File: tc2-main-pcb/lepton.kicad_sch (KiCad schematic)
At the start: 34 parts, among them U110 TD6810, U111 TD6810, U112 ME6216A28XG, U113 3N25000G33YC, U114 Flir_LEPTON

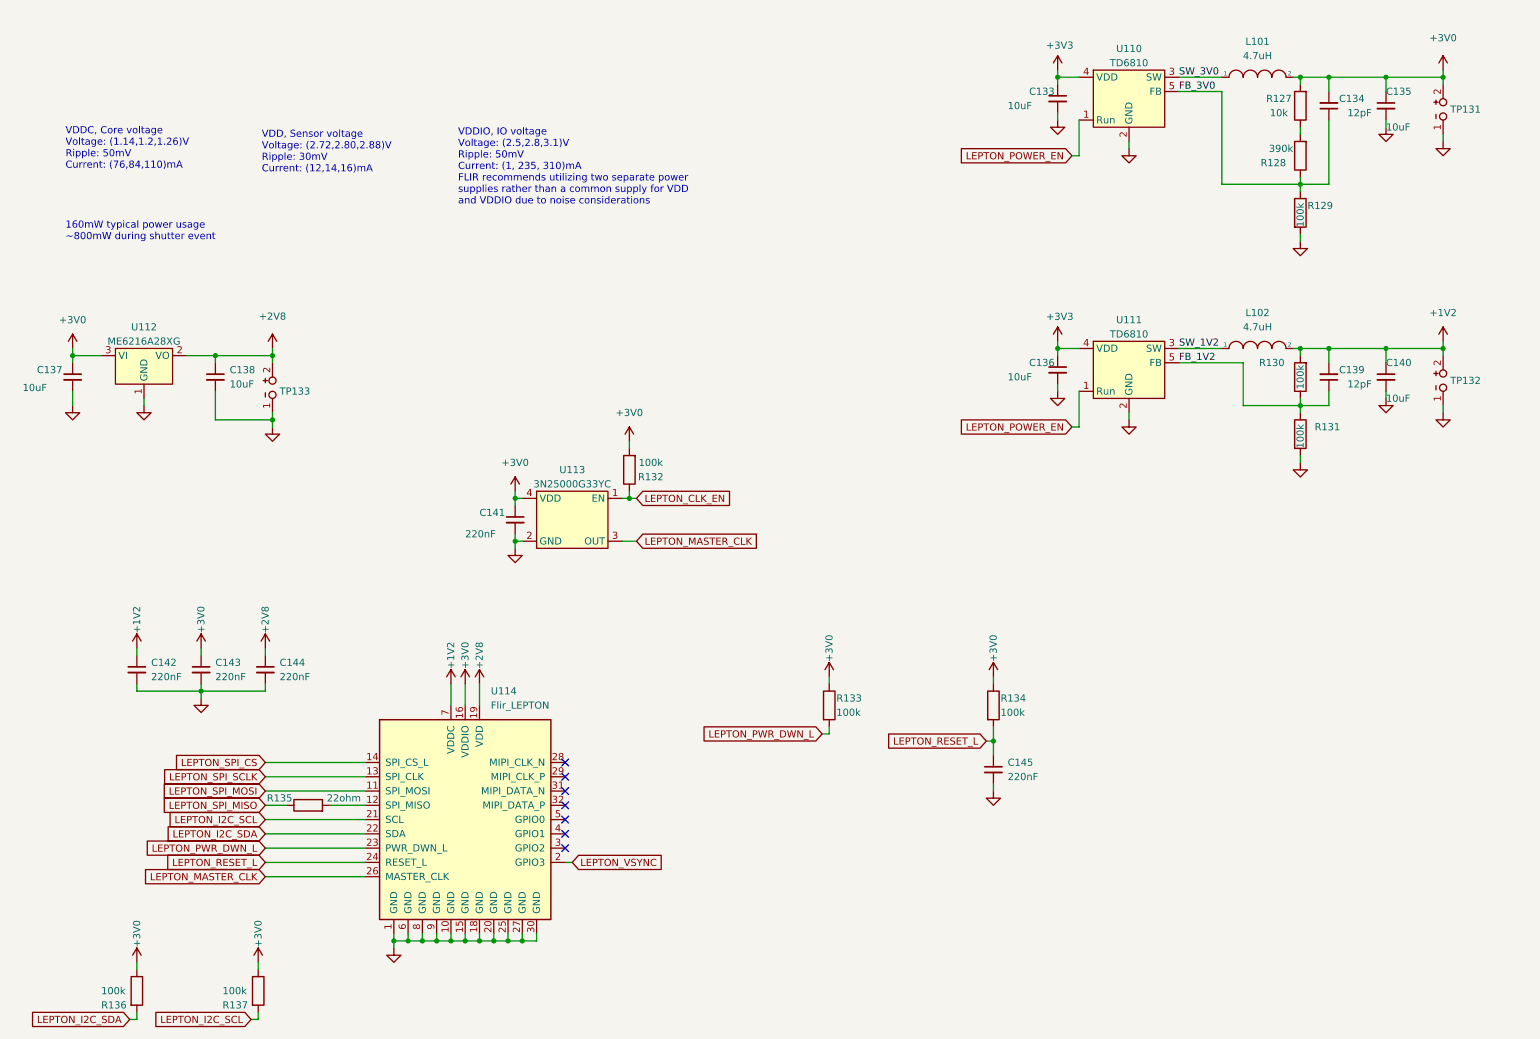
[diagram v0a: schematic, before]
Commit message: v0.7.2 panelise microphone boards
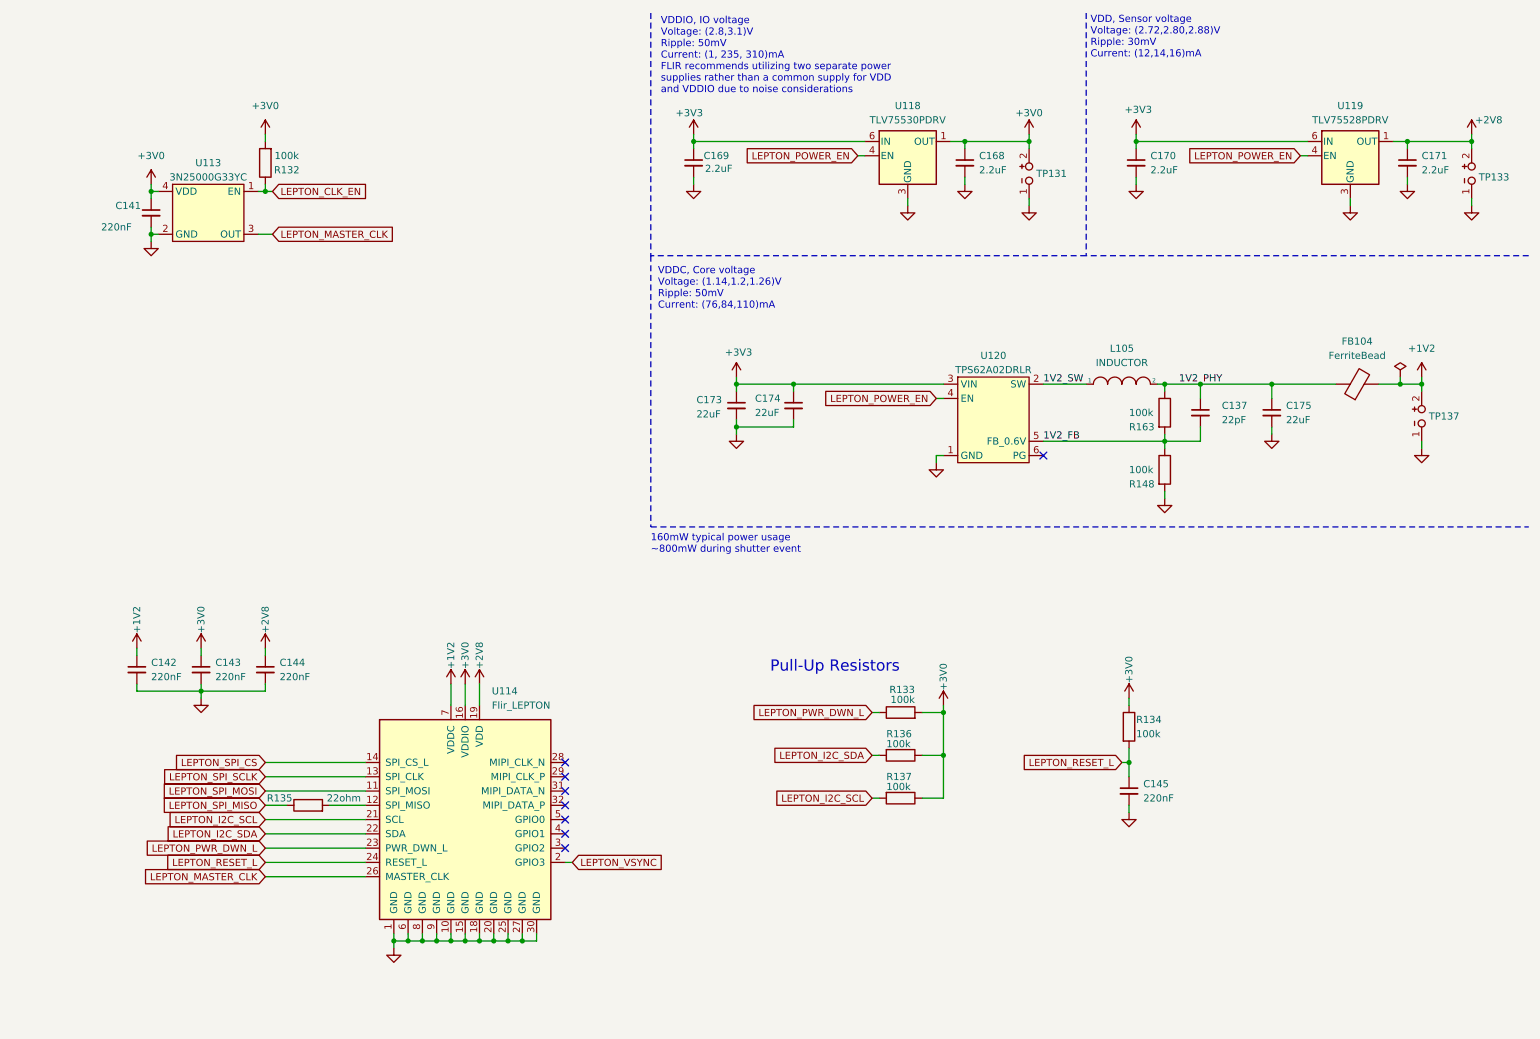
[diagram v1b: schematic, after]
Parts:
- removed C133, C135, C136, C138, C140: 10uF, Capacitor_SMD:C_0603_1608Metric, symbol Device:C_Small
- removed C134, C139: 12pF, Capacitor_SMD:C_0402_1005Metric, symbol Device:C_Small
- removed L101, L102: 4.7uH, cacophony-library:IND-SMD_L4.0-W4.0_SWPA4018S, symbol cacophony-library:Power_Inductor
- removed R127: 10k, Resistor_SMD:R_0402_1005Metric, symbol Device:R
- removed R128: 390k, Resistor_SMD:R_0402_1005Metric, symbol Device:R
- removed R129, R130, R131: 100k, Resistor_SMD:R_0402_1005Metric, symbol Device:R
- removed TP132: TP_2P, cacophony-library:test-point-2p, symbol cacophony-library:TestPoint_2Pole
- removed U110, U111: TD6810, cacophony-library:TSOT-23-5, symbol cacophony-library:TD6810
- removed U112: ME6216A28XG, Package_TO_SOT_SMD:TSOT-23, symbol cacophony-library:ME6216A28XG
- added C168, C169, C170, C171: 2.2uF, Capacitor_SMD:C_0402_1005Metric, symbol Device:C_Small
- added C173, C174, C175: 22uF, Capacitor_SMD:C_0603_1608Metric, symbol Device:C_Small
- added FB104: FerriteBead, Inductor_SMD:L_0805_2012Metric, symbol Device:FerriteBead
- added L105: INDUCTOR, Inductor_SMD:L_1008_2520Metric, symbol cacophony-library:Power_Inductor
- added R148, R163: 100k, Resistor_SMD:R_0402_1005Metric, symbol Device:R
- added TP137: TP_2P, cacophony-library:test-point-2p, symbol cacophony-library:TestPoint_2Pole
- added U118: TLV75530PDRV, Package_SON:WSON-6-1EP_2x2mm_P0.65mm_EP1x1.6mm, symbol Regulator_Linear:TLV75530PDRV
- added U119: TLV75528PDRV, Package_SON:WSON-6-1EP_2x2mm_P0.65mm_EP1x1.6mm, symbol Regulator_Linear:TLV75528PDRV
- added U120: TPS62A02DRLR, Package_TO_SOT_SMD:SOT-563, symbol cacophony-library:TPS62A02DRLR
- C137: value 10uF -> 22pF; footprint Capacitor_SMD:C_0603_1608Metric -> Capacitor_SMD:C_0402_1005Metric; LCSC C19702 -> C1555
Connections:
- net +1V2: now also FB104.2, TP137.2
- net +2V8: now also C171.1, U119.1 (OUT)
- net +3V0: now also R133.2, C168.1, U118.1 (OUT); no longer C137.1, R133.1
- net +3V3: now also C169.1, C170.1, C173.1, C174.1, U118.6 (IN), U119.6 (IN), U120.3 (VIN)
- net GND: now also C168.2, C169.2, C170.2, C171.2, C173.2, C174.2, C175.2, R148.2, TP137.1, U118.3 (GND), U118.7 (GND), U119.3 (GND), U119.7 (GND), U120.1 (GND); no longer C137.2
- net LEPTON_POWER_EN: now also U118.4 (EN), U119.4 (EN), U120.4 (EN)
- net LEPTON_PWR_DWN_L: now also R133.1; no longer R133.2
- new net 1V2_FB: C137.2, R148.1, R163.2, U120.5 (FB_0.6V)
- new net 1V2_PHY: C137.1, C175.1, FB104.1, L105.2, R163.1
- new net 1V2_SW: L105.1, U120.2 (SW)
- no-connect marks 7 -> 8
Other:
- note added: "Pull-Up Resistors"
- note added: "VDDIO, IO voltage Voltage: (2.8,3.1)V Ripple: 50mV Current: (1, 235, 310)mA FLIR recommends utilizing two separate power supplies rather than a common supply for VDD and VDDIO due to noise considerations"
- note removed: "VDDIO, IO voltage Voltage: (2.5,2.8,3.1)V Ripple: 50mV Current: (1, 235, 310)mA FLIR recommends utilizing two separate power supplies rather than a common supply for VDD and VDDIO due to noise considerations"
- moved on the sheet: C141, C145, R132, R133, R134, R136, R137, TP131, TP133, U113

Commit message: v0.7.3
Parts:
- U118: LCSC (none) -> C2859948
- U119: LCSC (none) -> C2865214
- U120: LCSC (none) -> C5350187

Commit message: 0.8.0 WIP
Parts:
- R135: value 22ohm -> 22Ω
- U120: footprint Package_TO_SOT_SMD:SOT-563 -> cacophony-library:SOT-563
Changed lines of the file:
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@@
 	(label "1V2_SW"
 		(at 198.12 78.74 0)
-		(fields_autoplaced yes)
 		(effects
 			(font
@@
 	(label "1V2_PHY"
 		(at 222.25 78.74 0)
-		(fields_autoplaced yes)
 		(effects
 			(font
@@
 	(label "1V2_FB"
 		(at 198.12 88.9 0)
-		(fields_autoplaced yes)
 		(effects
 			(font
@@
 			)
 		)
-		(property "Footprint" "Package_TO_SOT_SMD:SOT-563"
+		(property "Footprint" "cacophony-library:SOT-563"
 			(at 189.23 77.47 0)
 			(effects
@@
 			)
 		)
-		(property "Value" "22ohm"
+		(property "Value" "22Ω"
 			(at 73.66 152.4 90)
 			(effects
